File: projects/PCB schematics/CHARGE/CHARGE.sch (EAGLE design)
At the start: 16 parts, among them Q1 IRLZ44Z, Q2 IRLZ44Z, X1 5566-2, X2 5566-6, X3 5566-2

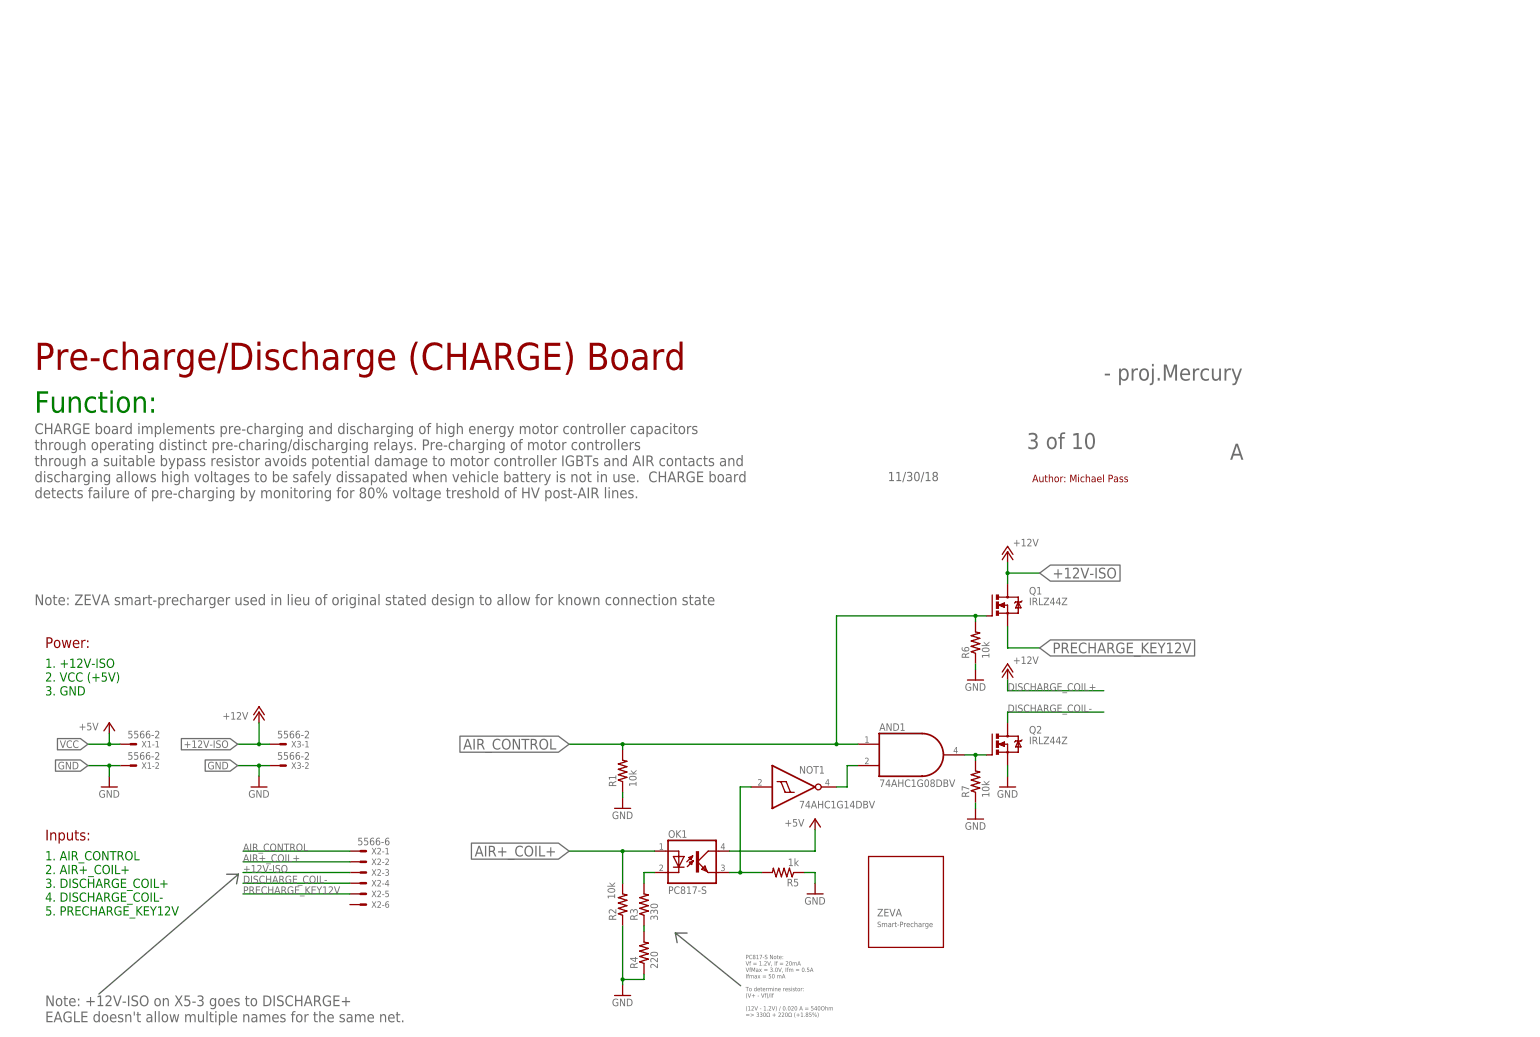
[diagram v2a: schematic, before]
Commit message: CHARGE - PR#2 requests made per @rgoedken.
- Third mosfet added in.
- Connector expanded to 8 pin
- AIR+/- added in
- Short device used to handle connections to power rail
- 5A fuse added in. 885 makes 5A.
- 100 ohm gate resistors added into three mosfets.
- DRC/ERC errors checked.

Squash - CHARGE - Final PR revisions.

Squash - CHARGE - Changed resistor values to allow 30mA instead of 20mA.
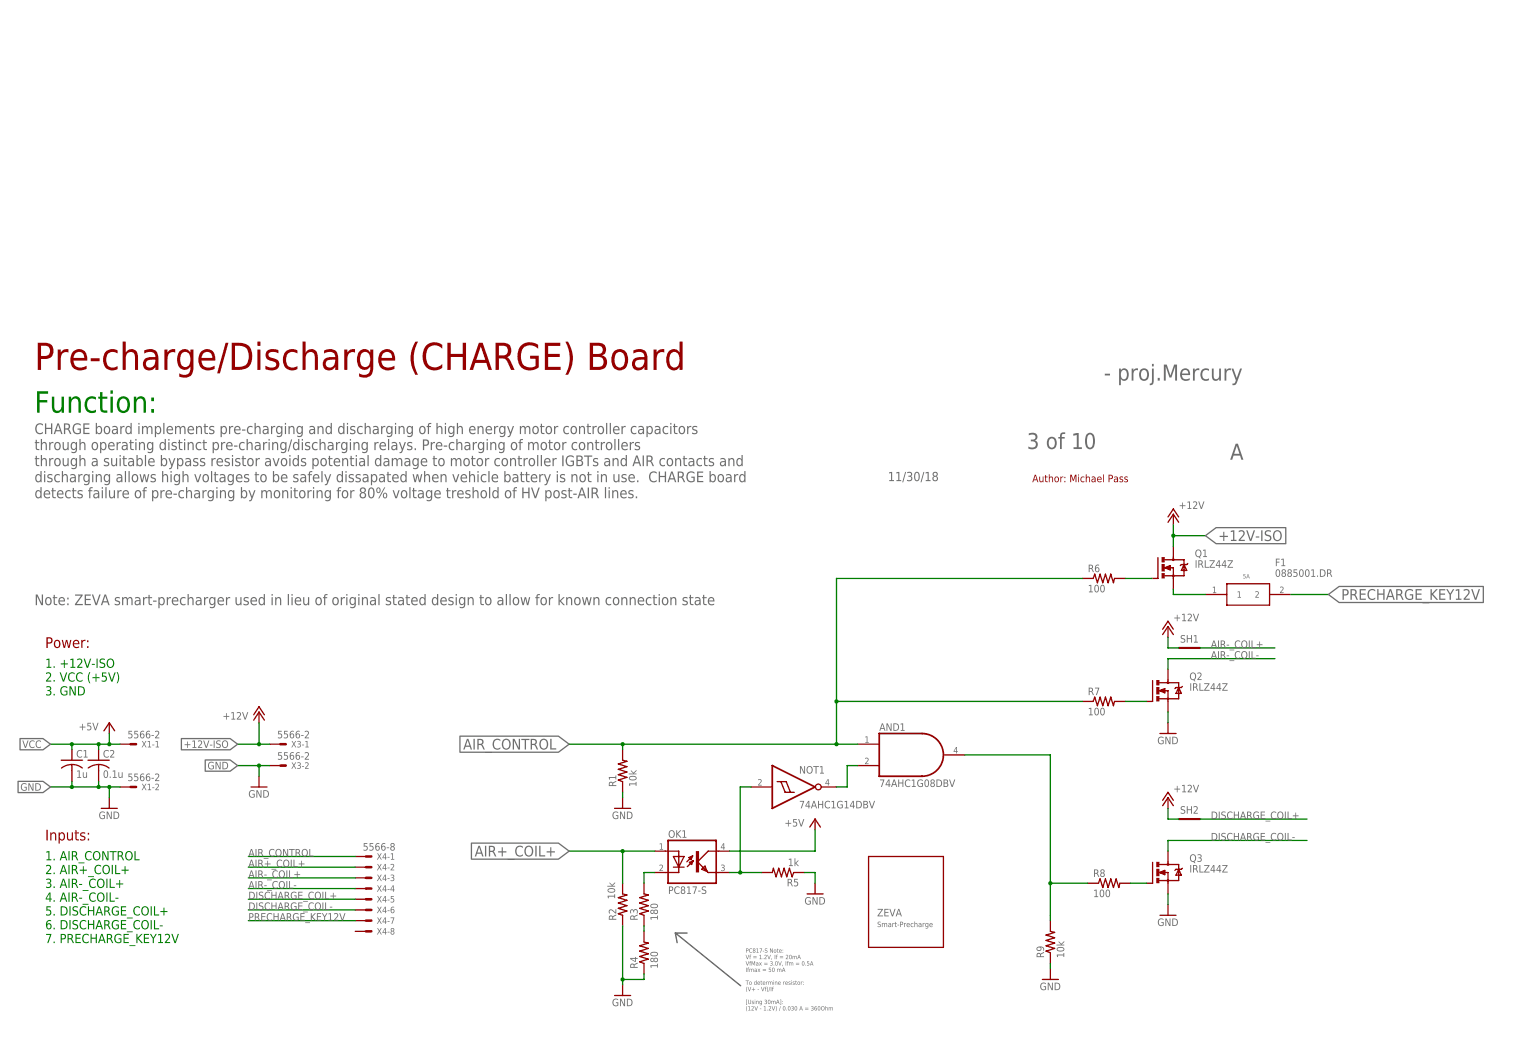
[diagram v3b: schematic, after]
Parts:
- removed X2: 5566-6, con-molex:5566-6
- added C1: 1u, rcl:C-USC0805
- added C2: 0.1u, rcl:C-USC0805
- added F1: 0885001.DR, 0885001.DR:0885001.DR
- added Q3: IRLZ44Z, transistor-power:IRLZ44Z
- added R8: 100, rcl:R-US_R0805
- added R9: 10k, rcl:R-US_R0805
- added SH1, SH2: SHORTA5, shorts:SHORTA5
- added X4: 5566-8, con-molex:5566-8
- R3: value 330 -> 180
- R4: value 220 -> 180
- R6, R7: value 10k -> 100
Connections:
- new net AIR-_COIL+: SH1.P$2, X4-3.S
- new net AIR-_COIL-: Q2.D, X4-4.S
- new net DISCHARGE_COIL+: SH2.P$2, X4-5.S
- new net N$1: Q3.G, R8.2
- new net N$2: Q1.G, R6.2
- new net N$4: Q2.G, R7.2
- new net PRE-FUSE_PRECHARGE_KEY12V: F1.1, Q1.S
- net +12V-ISO: now also SH1.P$1, SH2.P$1; no longer X2-3.S
- net AIR+_COIL+: now also X4-2.S; no longer X2-2.S
- net AIR_CONTROL: now also R6.1, R7.1, X4-1.S; no longer Q1.G, R6.2, X2-1.S
- net DISCHARGE_COIL-: now also Q3.D, X4-6.S; no longer Q2.D, X2-4.S
- net DISCHARGE_MOSFET: now also R8.1, R9.2; no longer Q2.G, R7.2
- net GND: now also C1.2, C2.2, Q3.S, R9.1; no longer R6.1, R7.1
- net PRECHARGE_KEY12V: now also F1.2, X4-7.S; no longer Q1.S, X2-5.S
- net VCC: now also C1.1, C2.1
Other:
- note added: "1. AIR_CONTROL 2. AIR+_COIL+ 3. AIR-_COIL+ 4. AIR-_COIL- 5. DISCHARGE_COIL+ 6. DISCHARGE_COIL- 7. PRECHARGE_KEY12V"
- note added: "5A"
- note added: "PC817-S Note: Vf = 1.2V, If = 20mA VfMax = 3.0V, Ifm = 0.5A Ifmax = 50 mA To determine resistor: (V+ - Vf)/If [Using 30mA]: (12V - 1.2V) / 0.030 A = 360Ohm"
- note removed: "1. AIR_CONTROL 2. AIR+_COIL+ 3. DISCHARGE_COIL+ 4. DISCHARGE_COIL- 5. PRECHARGE_KEY12V"
- note removed: "Note: +12V-ISO on X5-3 goes to DISCHARGE+ EAGLE doesn't allow multiple names for the same net."
- note removed: "PC817-S Note: Vf = 1.2V, If = 20mA VfMax = 3.0V, Ifm = 0.5A Ifmax = 50 mA To determine resistor: (V+ - Vf)/If (12V - 1.2V) / 0.020 A = 540Ohm => 330Ω + 220Ω (+1.85%)"
- moved on the sheet: Q1, Q2, R6, R7, X1-2

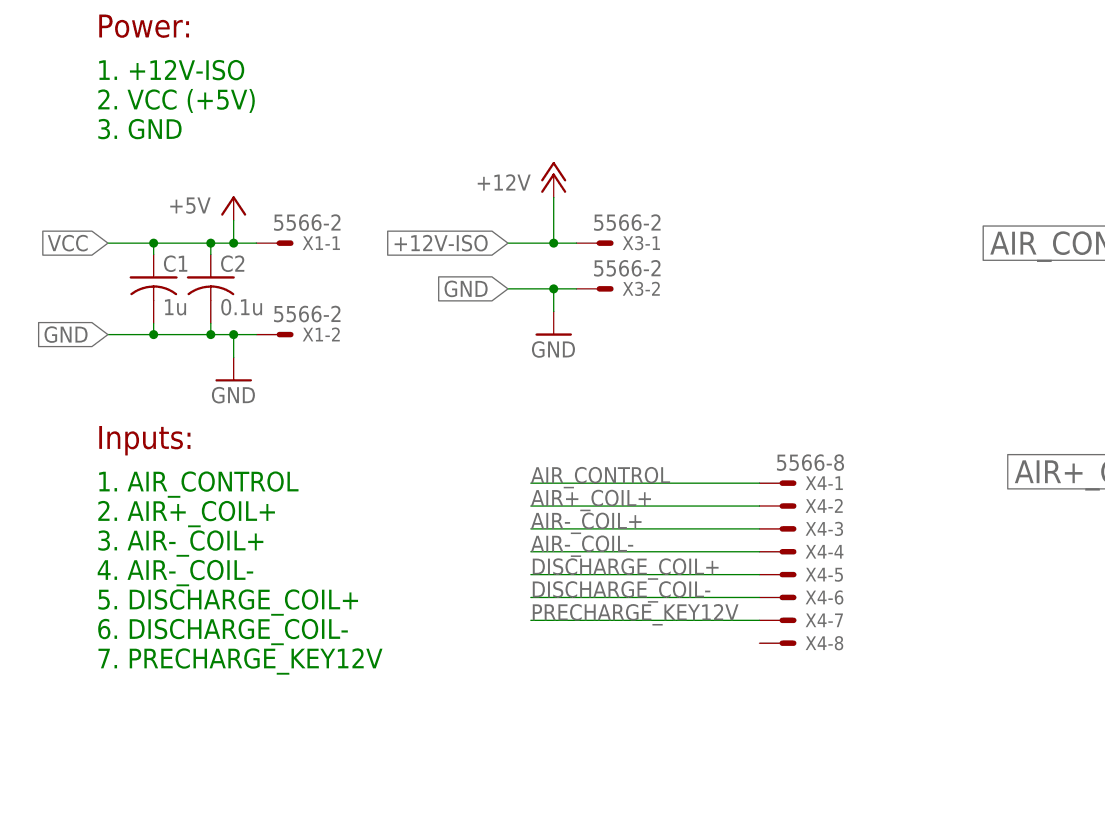
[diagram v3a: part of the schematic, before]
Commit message: PROJ - Silkscreen modifications - 50%.
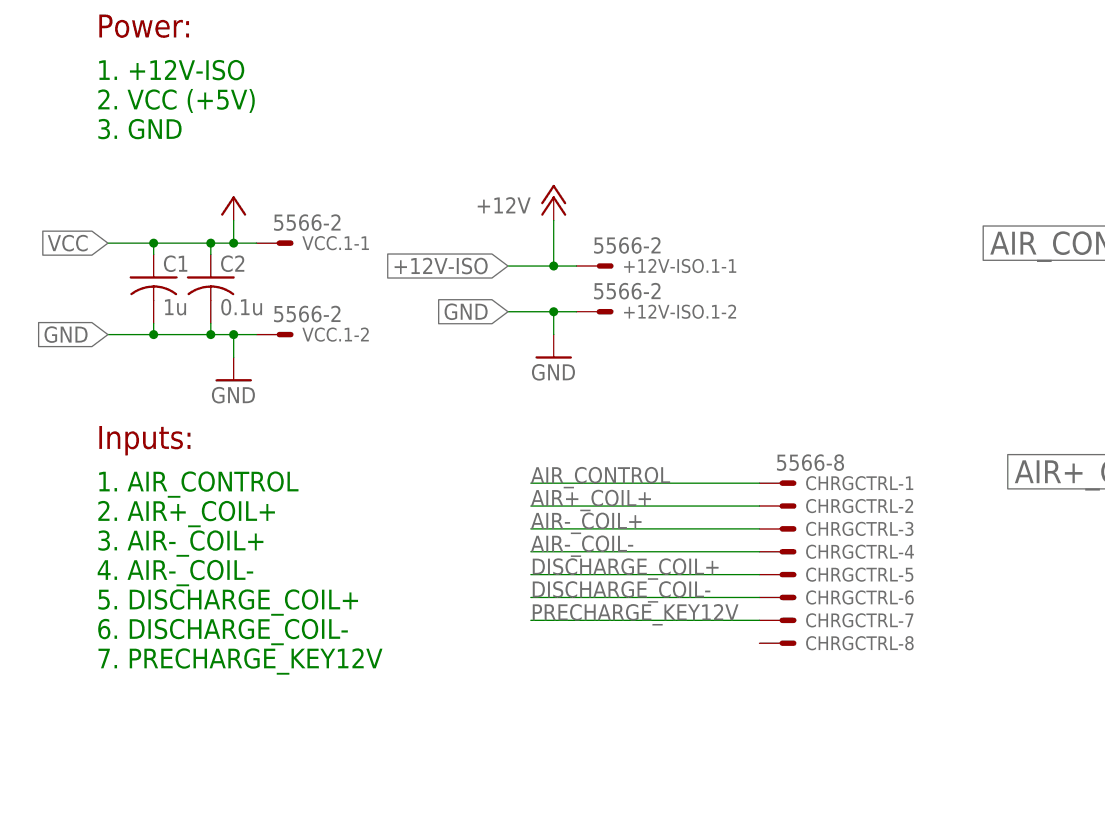
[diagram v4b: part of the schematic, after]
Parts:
- removed X3: 5566-2, con-molex:5566-2
- added +12V-ISO.1: 5566-2, con-molex:5566-2
- renumbered X1 to VCC.1, X4 to CHRGCTRL
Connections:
- net +12V-ISO: now also +12V-ISO.1-1.S; no longer X3-1.S
- net GND: now also +12V-ISO.1-2.S; no longer X3-2.S
